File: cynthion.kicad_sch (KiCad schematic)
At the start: 26 parts, among them J1 USB_C, J11 SPRING_CONTACT, J12 SPRING_CONTACT, J13 SPRING_CONTACT, J14 SPRING_CONTACT, J15 SPRING_CONTACT, J16 SPRING_CONTACT, J2 USB_C, J3 USB_A, J4 USB_C, J7 PMOD_A, J8 PMOD_B, SW1 BTN_PROGRAM, SW2 BTN_RESET, SW3 BTN_USER

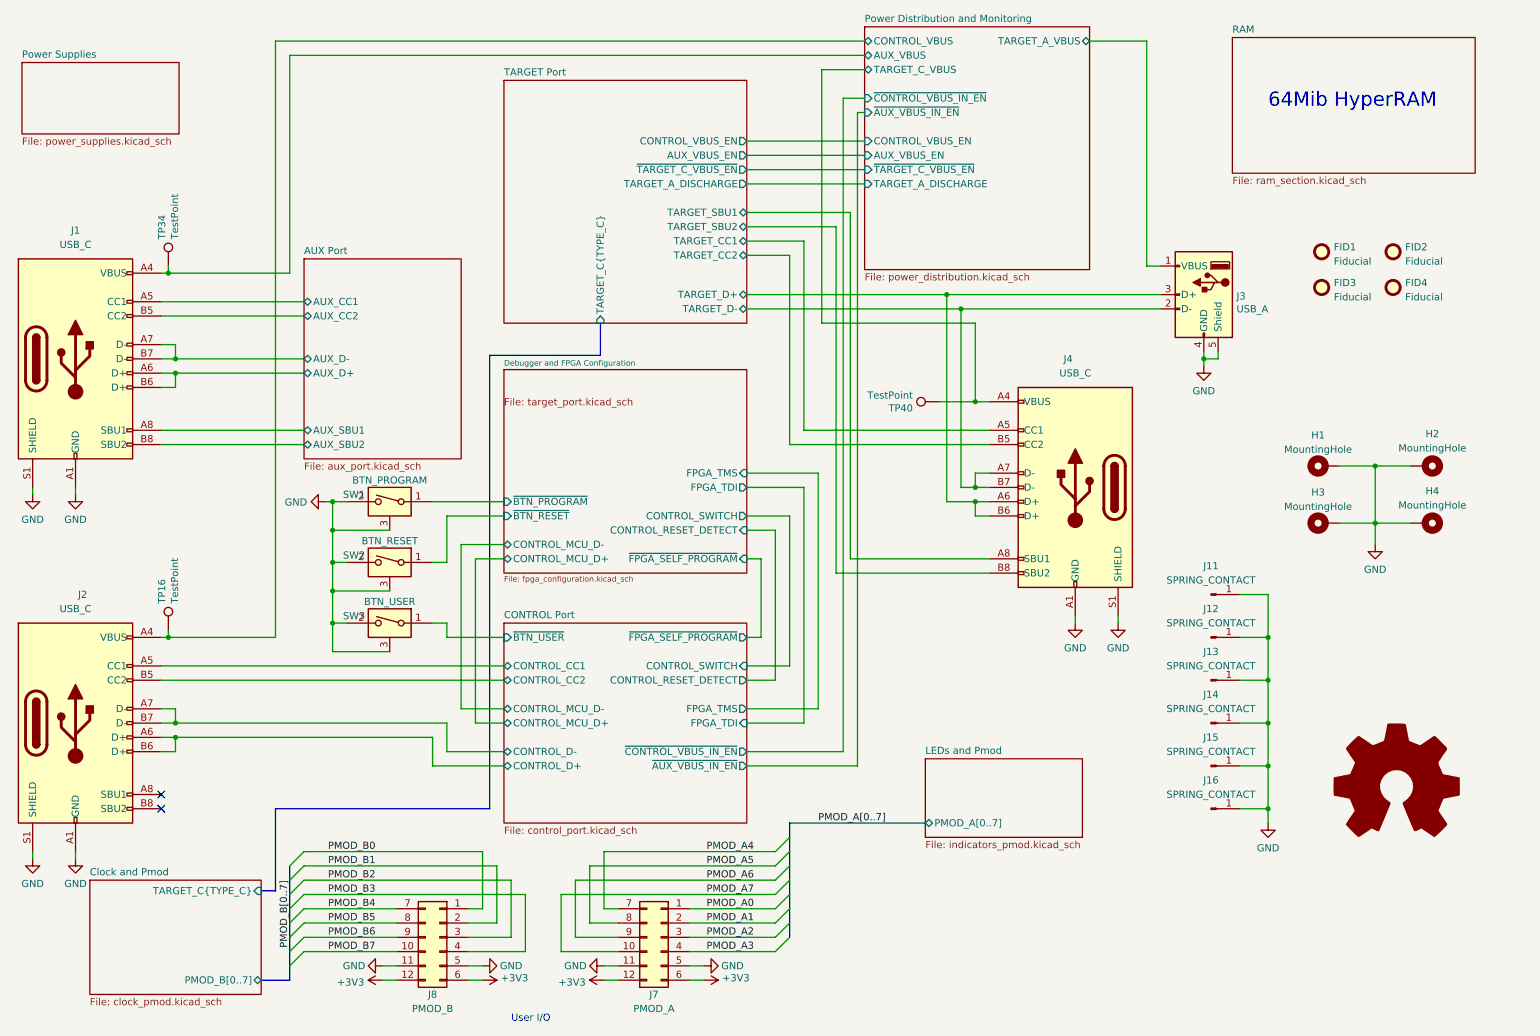
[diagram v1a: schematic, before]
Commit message: Rearrange schematic for readability
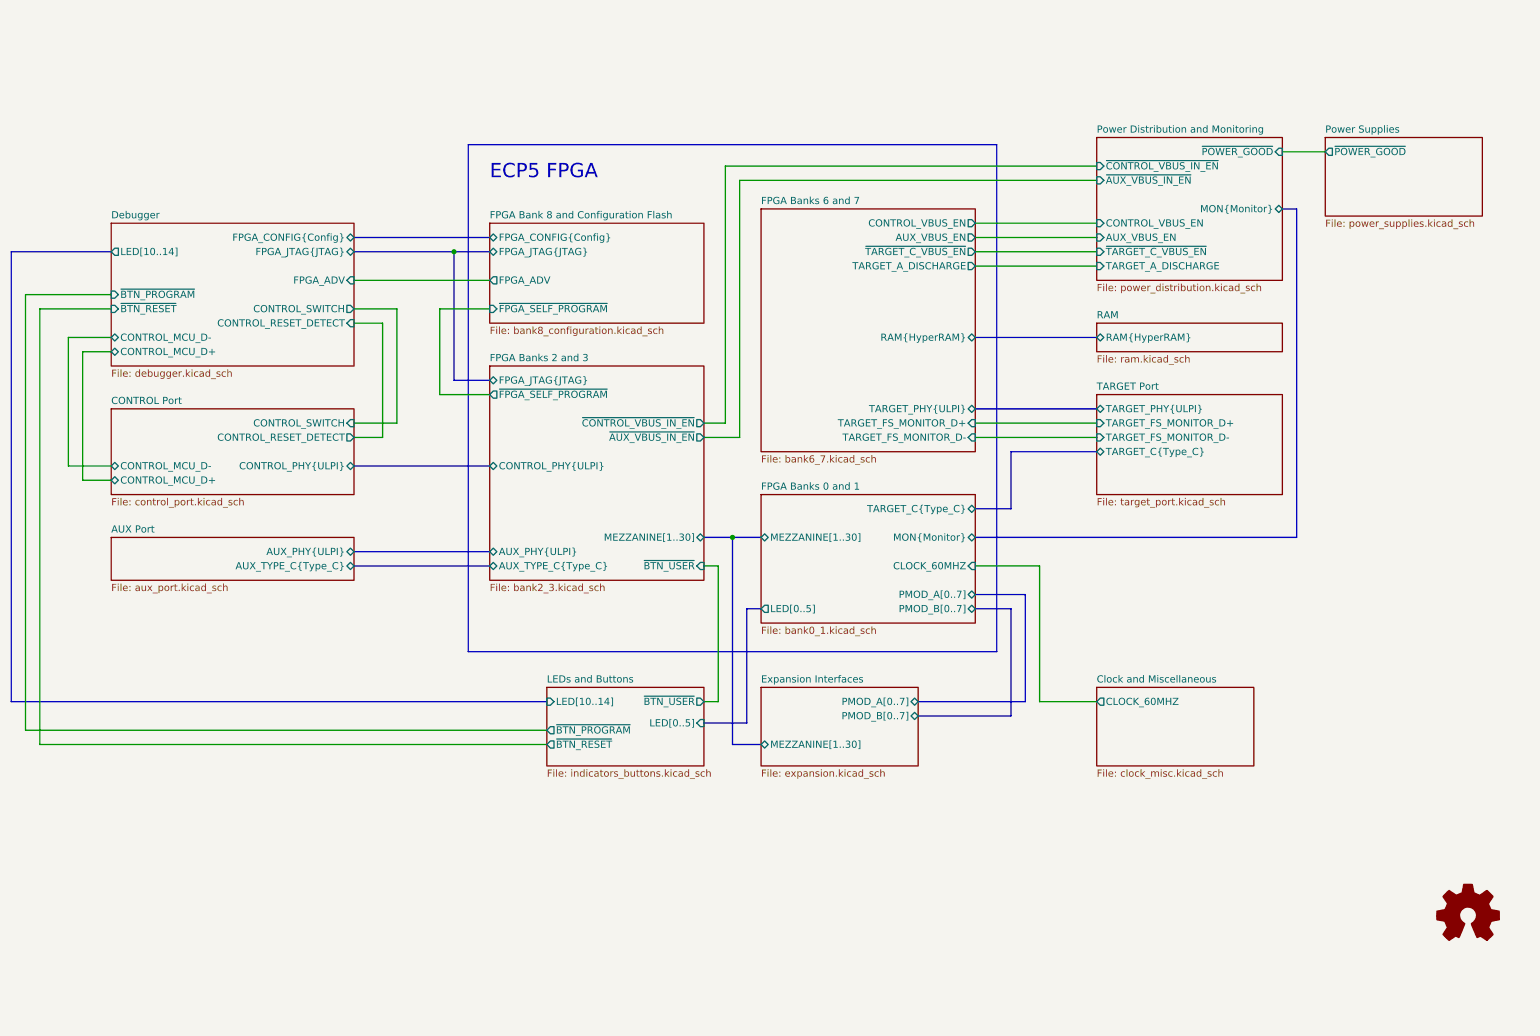
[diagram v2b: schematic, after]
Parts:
- removed FID1, FID2, FID3, FID4: Fiducial, Fiducial:Fiducial_0.5mm_Mask1mm, symbol Mechanical:Fiducial
- removed H1, H2, H3, H4: MountingHole, MountingHole:MountingHole_2.2mm_M2_Pad_Via, symbol Mechanical:MountingHole_Pad
- removed J1, J2, J4: USB_C, cynthion:USB_C_Receptacle_HRO_TYPE-C-31-M-12, symbol Connector:USB_C_Receptacle_USB2.0
- removed J11, J12, J13, J14, J15, J16: SPRING_CONTACT, cynthion:BW0033AG-L3.4W0.9H1.8, symbol Connector:Conn_01x01_Male
- removed J3: USB_A, cynthion:USB_A_Kycon_KUSBXHT-SB-AS1N-B30-NF_Horizontal, symbol Connector:USB_A
- removed J7: PMOD_A, cynthion:PinSocket_2x06_P2.54mm_PMOD, symbol Connector_Generic:Conn_02x06_Top_Bottom
- removed J8: PMOD_B, cynthion:PinSocket_2x06_P2.54mm_PMOD, symbol Connector_Generic:Conn_02x06_Top_Bottom
- removed SW1: BTN_PROGRAM, cynthion:SW_Tactile_SPST_Angled_TC-1109DE-B-F, symbol support_hardware:SW_SPST_shielded
- removed SW2: BTN_RESET, cynthion:SW_Tactile_SPST_Angled_TC-1109DE-B-F, symbol support_hardware:SW_SPST_shielded
- removed SW3: BTN_USER, cynthion:SW_Tactile_SPST_Angled_TC-1109DE-B-F, symbol support_hardware:SW_SPST_shielded
- removed TP16, TP34, TP40: TestPoint, TestPoint:TestPoint_Pad_D1.0mm, symbol Connector:TestPoint
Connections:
- no-connect marks 2 -> 0
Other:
- sheet Debugger and FPGA Configuration renamed Debugger
- removed sheet Clock and Pmod
- removed sheet LEDs and Pmod
- added sheet Clock and Miscellaneous (clock_misc.kicad_sch)
- added sheet Expansion Interfaces (expansion.kicad_sch)
- added sheet FPGA Bank 8 and Configuration Flash (bank8_configuration.kicad_sch)
- added sheet FPGA Banks 0 and 1 (bank0_1.kicad_sch)
- added sheet FPGA Banks 2 and 3 (bank2_3.kicad_sch)
- added sheet FPGA Banks 6 and 7 (bank6_7.kicad_sch)
- added sheet LEDs and Buttons (indicators_buttons.kicad_sch)
- sheet AUX Port ports: added AUX_PHY{ULPI}, AUX_TYPE_C{Type_C}; removed AUX_CC1, AUX_CC2, AUX_D+, AUX_D-, AUX_SBU1, AUX_SBU2
- sheet CONTROL Port ports: added CONTROL_PHY{ULPI}; removed CONTROL_CC1, CONTROL_CC2, CONTROL_D+, CONTROL_D-, FPGA_TDI, FPGA_TMS, ~{AUX_VBUS_IN_EN}, ~{BTN_USER}, ~{CONTROL_VBUS_IN_EN}, ~{FPGA_SELF_PROGRAM}
- sheet Debugger: file fpga_configuration.kicad_sch -> debugger.kicad_sch
- sheet Debugger ports: added FPGA_ADV, FPGA_CONFIG{Config}, FPGA_JTAG{JTAG}, LED[10..14]; removed FPGA_TDI, FPGA_TMS, ~{FPGA_SELF_PROGRAM}
- sheet Power Distribution and Monitoring ports: added MON{Monitor}, ~{POWER_GOOD}; removed AUX_VBUS, CONTROL_VBUS, TARGET_A_VBUS, TARGET_C_VBUS
- sheet Power Supplies ports: added ~{POWER_GOOD}; removed none
- sheet RAM: file ram_section.kicad_sch -> ram.kicad_sch
- sheet RAM ports: added RAM{HyperRAM}; removed none
- sheet TARGET Port ports: added TARGET_C{Type_C}, TARGET_FS_MONITOR_D+, TARGET_FS_MONITOR_D-, TARGET_PHY{ULPI}; removed AUX_VBUS_EN, CONTROL_VBUS_EN, TARGET_A_DISCHARGE, TARGET_CC1, TARGET_CC2, TARGET_C{TYPE_C}, TARGET_D+, TARGET_D-, TARGET_SBU1, TARGET_SBU2, ~{TARGET_C_VBUS_EN}
- note added: "ECP5 FPGA"
- note removed: "64Mib HyperRAM"
- note removed: "User I/O"

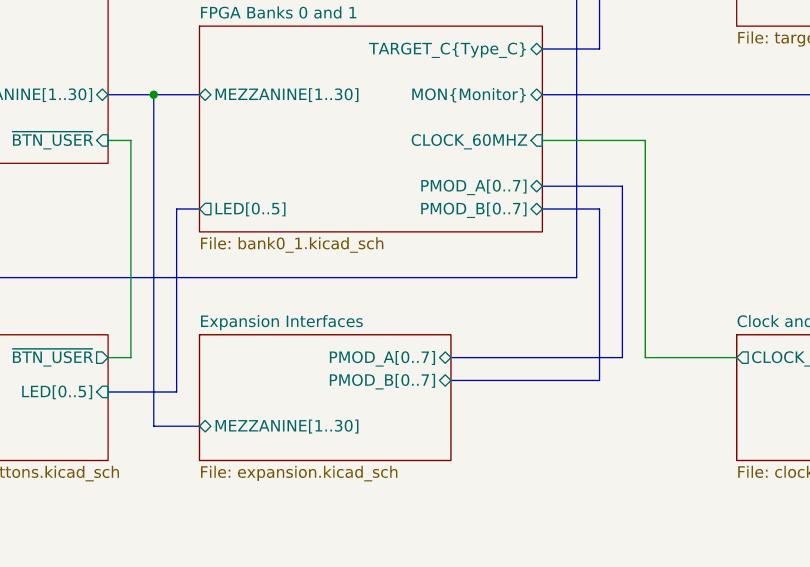
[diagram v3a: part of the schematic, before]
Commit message: Clean up schematic
- Renumber Pmod signal names to match silkscreen labels
- Clean up FPGA symbol
- Clean up PHY symbol
- Add title block to newer sheets
- Fix horizontal line in LED sheet
- Improve various label positions
- Update data sheet fields
- Renumber pages
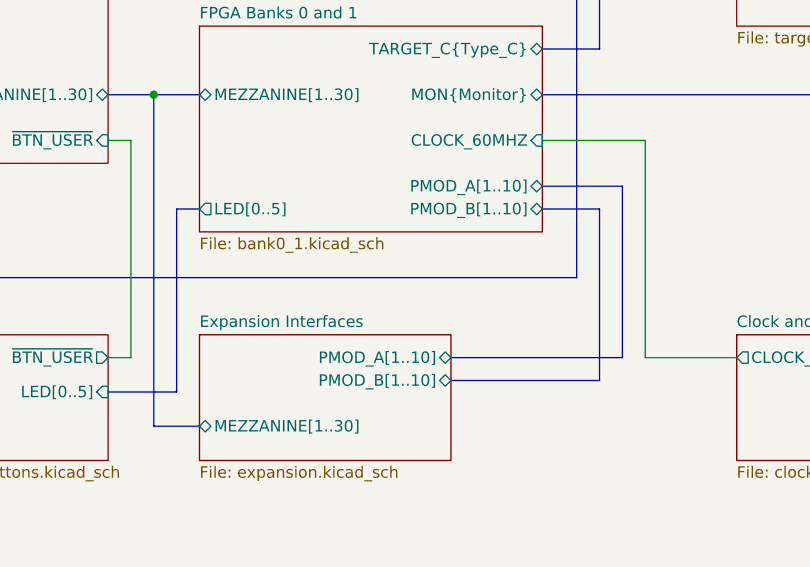
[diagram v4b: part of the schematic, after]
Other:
- sheet Expansion Interfaces ports: added PMOD_A[1..10], PMOD_B[1..10]; removed PMOD_A[0..7], PMOD_B[0..7]
- sheet FPGA Banks 0 and 1 ports: added PMOD_A[1..10], PMOD_B[1..10]; removed PMOD_A[0..7], PMOD_B[0..7]
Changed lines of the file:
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@@
     (instances
       (project "cynthion"
-        (path "/fb621148-8145-4217-9712-738e1b5a4823" (page "8"))
+        (path "/fb621148-8145-4217-9712-738e1b5a4823" (page "18"))
       )
     )
@@
     (instances
       (project "cynthion"
-        (path "/fb621148-8145-4217-9712-738e1b5a4823" (page "5"))
+        (path "/fb621148-8145-4217-9712-738e1b5a4823" (page "17"))
       )
     )
@@
     (instances
       (project "cynthion"
-        (path "/fb621148-8145-4217-9712-738e1b5a4823" (page "6"))
+        (path "/fb621148-8145-4217-9712-738e1b5a4823" (page "2"))
       )
     )
@@
     (instances
       (project "cynthion"
-        (path "/fb621148-8145-4217-9712-738e1b5a4823" (page "3"))
+        (path "/fb621148-8145-4217-9712-738e1b5a4823" (page "4"))
       )
     )
@@
     (instances
       (project "cynthion"
-        (path "/fb621148-8145-4217-9712-738e1b5a4823" (page "4"))
+        (path "/fb621148-8145-4217-9712-738e1b5a4823" (page "7"))
       )
     )
@@
     (instances
       (project "cynthion"
-        (path "/fb621148-8145-4217-9712-738e1b5a4823" (page "9"))
+        (path "/fb621148-8145-4217-9712-738e1b5a4823" (page "14"))
       )
     )
@@
     (instances
       (project "cynthion"
-        (path "/fb621148-8145-4217-9712-738e1b5a4823" (page "7"))
+        (path "/fb621148-8145-4217-9712-738e1b5a4823" (page "12"))
       )
     )
@@
     (instances
       (project "cynthion"
-        (path "/fb621148-8145-4217-9712-738e1b5a4823" (page "10"))
+        (path "/fb621148-8145-4217-9712-738e1b5a4823" (page "19"))
       )
     )
@@
     (instances
       (project "cynthion"
-        (path "/fb621148-8145-4217-9712-738e1b5a4823" (page "2"))
+        (path "/fb621148-8145-4217-9712-738e1b5a4823" (page "11"))
       )
     )
@@
       (effects (font (size 1.27 1.27)) (justify left top))
     )
-    (pin "PMOD_B[0..7]" bidirectional (at 179.07 139.7 0)
-      (effects (font (size 1.27 1.27)) (justify right))
-    )
-    (pin "PMOD_A[0..7]" bidirectional (at 179.07 137.16 0)
-      (effects (font (size 1.27 1.27)) (justify right))
-    )
     (pin "MEZZANINE[1..30]" bidirectional (at 151.13 144.78 180)
       (effects (font (size 1.27 1.27)) (justify left))
     )
+    (pin "PMOD_A[1..10]" bidirectional (at 179.07 137.16 0)
+      (effects (font (size 1.27 1.27)) (justify right))
+    )
+    (pin "PMOD_B[1..10]" bidirectional (at 179.07 139.7 0)
+      (effects (font (size 1.27 1.27)) (justify right))
+    )
     (instances
       (project "cynthion"
@@
     (instances
       (project "cynthion"
-        (path "/fb621148-8145-4217-9712-738e1b5a4823" (page "17"))
+        (path "/fb621148-8145-4217-9712-738e1b5a4823" (page "15"))
       )
     )
@@
       (effects (font (size 1.27 1.27)) (justify left top))
     )
-    (pin "PMOD_B[0..7]" bidirectional (at 189.23 120.65 0)
-      (effects (font (size 1.27 1.27)) (justify right))
-    )
     (pin "TARGET_C{Type_C}" bidirectional (at 189.23 102.87 0)
       (effects (font (size 1.27 1.27)) (justify right))
@@
       (effects (font (size 1.27 1.27)) (justify left))
     )
-    (pin "PMOD_A[0..7]" bidirectional (at 189.23 118.11 0)
-      (effects (font (size 1.27 1.27)) (justify right))
-    )
     (pin "MON{Monitor}" bidirectional (at 189.23 107.95 0)
       (effects (font (size 1.27 1.27)) (justify right))
     )
-    (instances
-      (project "cynthion"
-        (path "/fb621148-8145-4217-9712-738e1b5a4823" (page "18"))
+    (pin "PMOD_A[1..10]" bidirectional (at 189.23 118.11 0)
+      (effects (font (size 1.27 1.27)) (justify right))
+    )
+    (pin "PMOD_B[1..10]" bidirectional (at 189.23 120.65 0)
+      (effects (font (size 1.27 1.27)) (justify right))
+    )
+    (instances
+      (project "cynthion"
+        (path "/fb621148-8145-4217-9712-738e1b5a4823" (page "10"))
       )
     )
@@
     (instances
       (project "cynthion"
-        (path "/fb621148-8145-4217-9712-738e1b5a4823" (page "19"))
-      )
-    )
+        (path "/fb621148-8145-4217-9712-738e1b5a4823" (page "13"))
+      )
+    )

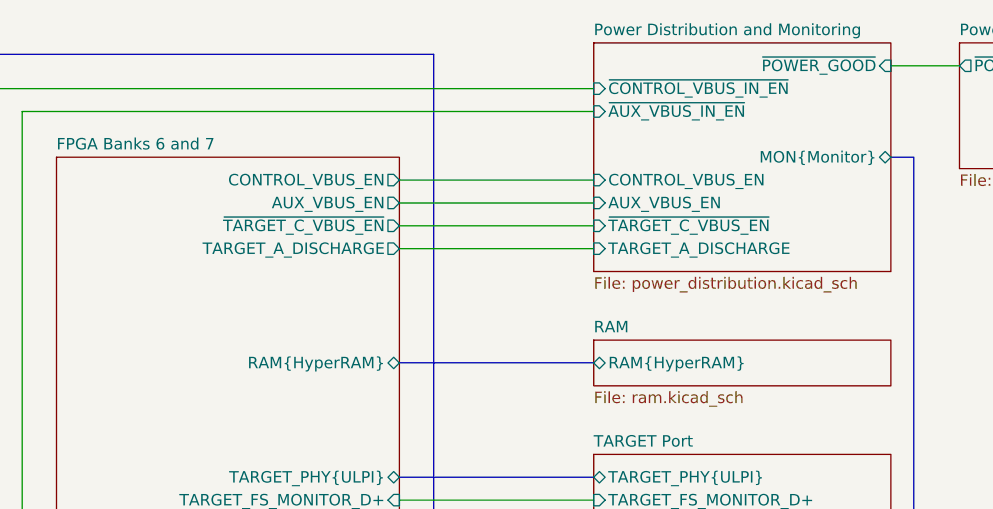
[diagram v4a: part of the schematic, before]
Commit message: Change TARGET_C_VBUS pass-through default
Previously pass-through power between TARGET C and TARGET A was enabled
by default, even when the Cynthion was unpowered. This had the potential
benefit of allowing a pass-through target device to function while the
Cynthion was off, but the feature was unreliable due to loading of D+/D-
by the PHY and TARGET_FS_MONITOR connections. All pass-through power is
now disabled by default, providing a consistent user experience while
the Cynthion is unpowered.
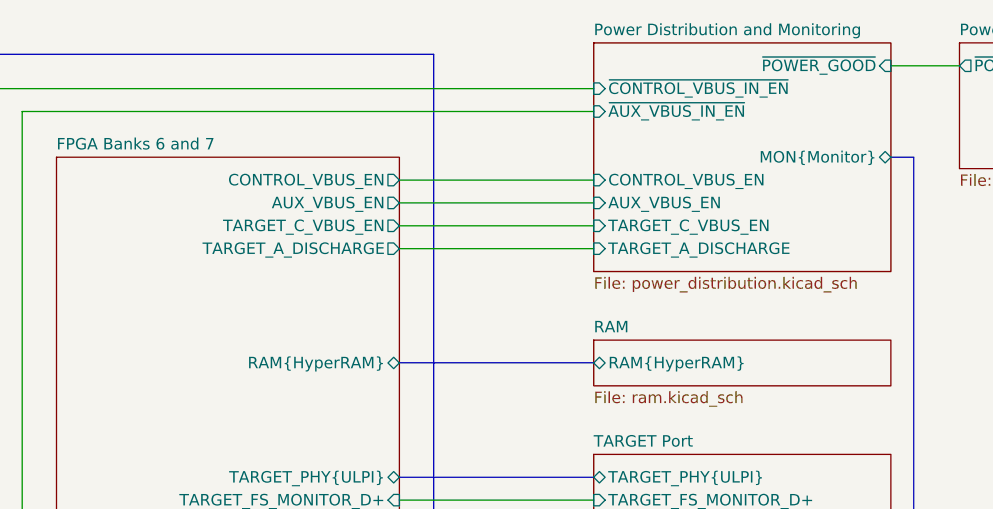
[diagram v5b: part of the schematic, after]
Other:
- sheet FPGA Banks 6 and 7 ports: added TARGET_C_VBUS_EN; removed ~{TARGET_C_VBUS_EN}
- sheet Power Distribution and Monitoring ports: added TARGET_C_VBUS_EN; removed ~{TARGET_C_VBUS_EN}
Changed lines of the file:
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@@
-      (effects (font (size 1.27 1.27)) (justify right))
-    )
-    (pin "~{TARGET_C_VBUS_EN}" output (at 189.23 57.15 0)
       (effects (font (size 1.27 1.27)) (justify right))
     )
@@
     )
     (pin "RAM{HyperRAM}" bidirectional (at 189.23 72.39 0)
+      (effects (font (size 1.27 1.27)) (justify right))
+    )
+    (pin "TARGET_C_VBUS_EN" output (at 189.23 57.15 0)
       (effects (font (size 1.27 1.27)) (justify right))
     )
@@
       (effects (font (size 1.27 1.27)) (justify left))
     )
-    (pin "~{TARGET_C_VBUS_EN}" input (at 210.82 57.15 180)
-      (effects (font (size 1.27 1.27)) (justify left))
-    )
     (pin "~{CONTROL_VBUS_IN_EN}" input (at 210.82 41.91 180)
       (effects (font (size 1.27 1.27)) (justify left))
@@
       (effects (font (size 1.27 1.27)) (justify right))
     )
+    (pin "TARGET_C_VBUS_EN" input (at 210.82 57.15 180)
+      (effects (font (size 1.27 1.27)) (justify left))
+    )
     (instances

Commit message: Update copyright notices
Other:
- company: Copyright 2019-2023 Great Scott Gadgets -> ${COPYRIGHT}
- title: Cynthion -> ${TITLE}
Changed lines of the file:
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@@
   (paper "A4")
   (title_block
-    (title "Cynthion")
+    (title "${TITLE}")
     (date "${DATE}")
     (rev "${VERSION}")
-    (company "Copyright 2019-2023 Great Scott Gadgets")
-    (comment 1 "Licensed under the CERN-OHL-P v2")
+    (company "${COPYRIGHT}")
+    (comment 1 "${LICENSE}")
   )
   (bus_alias "JTAG" (members "TMS" "TCK" "TDI" "TDO"))
